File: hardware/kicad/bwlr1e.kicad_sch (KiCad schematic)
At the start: 62 parts, among them J1 Qwiic, Q1 AO3407, Q2 DMG1012UW, SW3 RESET, SW4 BOOT, U1 BME688, U2 RAK3172, U3 AEM10941-QFN, U4 XC6215

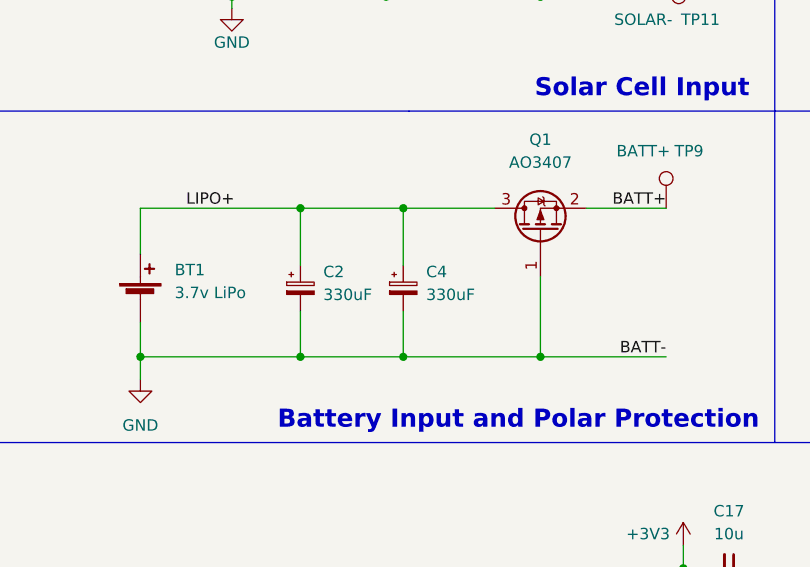
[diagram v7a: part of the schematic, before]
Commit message: rename value unit of components
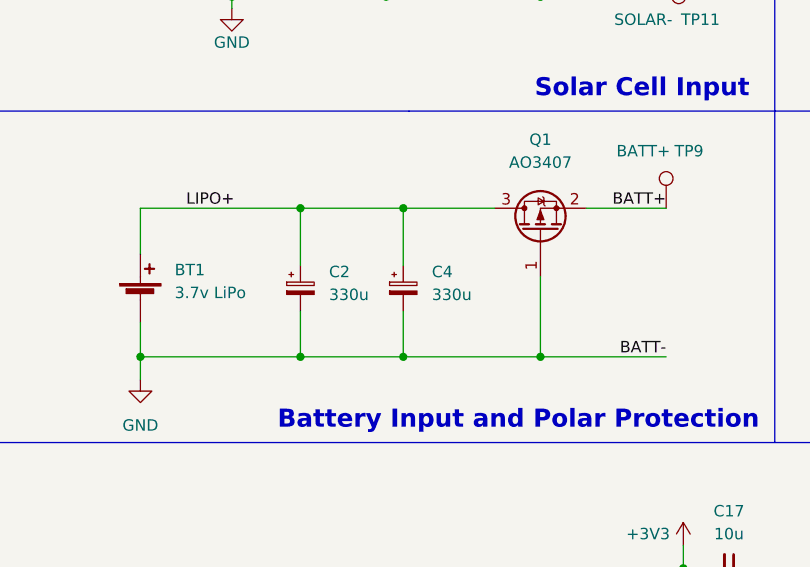
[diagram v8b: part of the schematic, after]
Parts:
- C2, C4: value 330uF -> 330u
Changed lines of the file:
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@@
   (symbol (lib_id "Device:C_Polarized_Small") (at 61.595 70.485 0) (unit 1)
     (in_bom yes) (on_board yes) (dnp no) (fields_autoplaced)
-    (property "Reference" "C4" (at 64.135 68.6688 0)
+    (property "Reference" "C4" (at 64.77 68.6689 0)
       (effects (font (size 1.27 1.27)) (justify left))
     )
-    (property "Value" "330uF" (at 64.135 71.2088 0)
+    (property "Value" "330u" (at 64.77 71.2089 0)
       (effects (font (size 1.27 1.27)) (justify left))
     )
@@
   (symbol (lib_id "Device:C_Polarized_Small") (at 50.165 70.485 0) (unit 1)
     (in_bom yes) (on_board yes) (dnp no) (fields_autoplaced)
-    (property "Reference" "C2" (at 52.705 68.6688 0)
+    (property "Reference" "C2" (at 53.34 68.6689 0)
       (effects (font (size 1.27 1.27)) (justify left))
     )
-    (property "Value" "330uF" (at 52.705 71.2088 0)
+    (property "Value" "330u" (at 53.34 71.2089 0)
       (effects (font (size 1.27 1.27)) (justify left))
     )
